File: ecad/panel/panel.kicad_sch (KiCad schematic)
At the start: 201 parts, among them J1 10145226-0241N13LF, J2 Conn_01x03_Pin, J3 USB4105-GF-A, J4 5017868090, SW1 SW_SPDT, SW10 SW_SPDT, SW11 SW_SPDT, SW12 SW_SPDT, SW13 SW_SPDT, SW14 SW_SPDT, SW15 SW_SPDT, SW16 SW_SPDT, SW17 SW_Push, SW18 SW_Push, SW19 SW_Push, SW2 SW_SPDT, SW20 SW_Push, SW21 SW_Push, SW22 SW_Push, SW23 SW_Push, SW24 SW_Push, SW25 SW_Push, SW26 SW_Push, SW27 SW_Push, SW28 SW_Push, SW29 SW_Push, SW3 SW_SPDT, SW30 SW_Push, SW31 SW_Push, SW4 SW_SPDT, SW5 SW_SPDT, SW6 SW_SPDT, SW7 SW_SPDT, SW8 SW_SPDT, SW9 SW_SPDT, U1 TLC59211IN, U2 TLC59211IN, U3 TLC59211IN, U4 TLC59211IN, U5 TLC59211IN, U6 RP2350_80QFN, U7 W25Q128JVS, U8 MCP23017_SO, U9 MCP23017_SO, X1 ABM8-272-T3

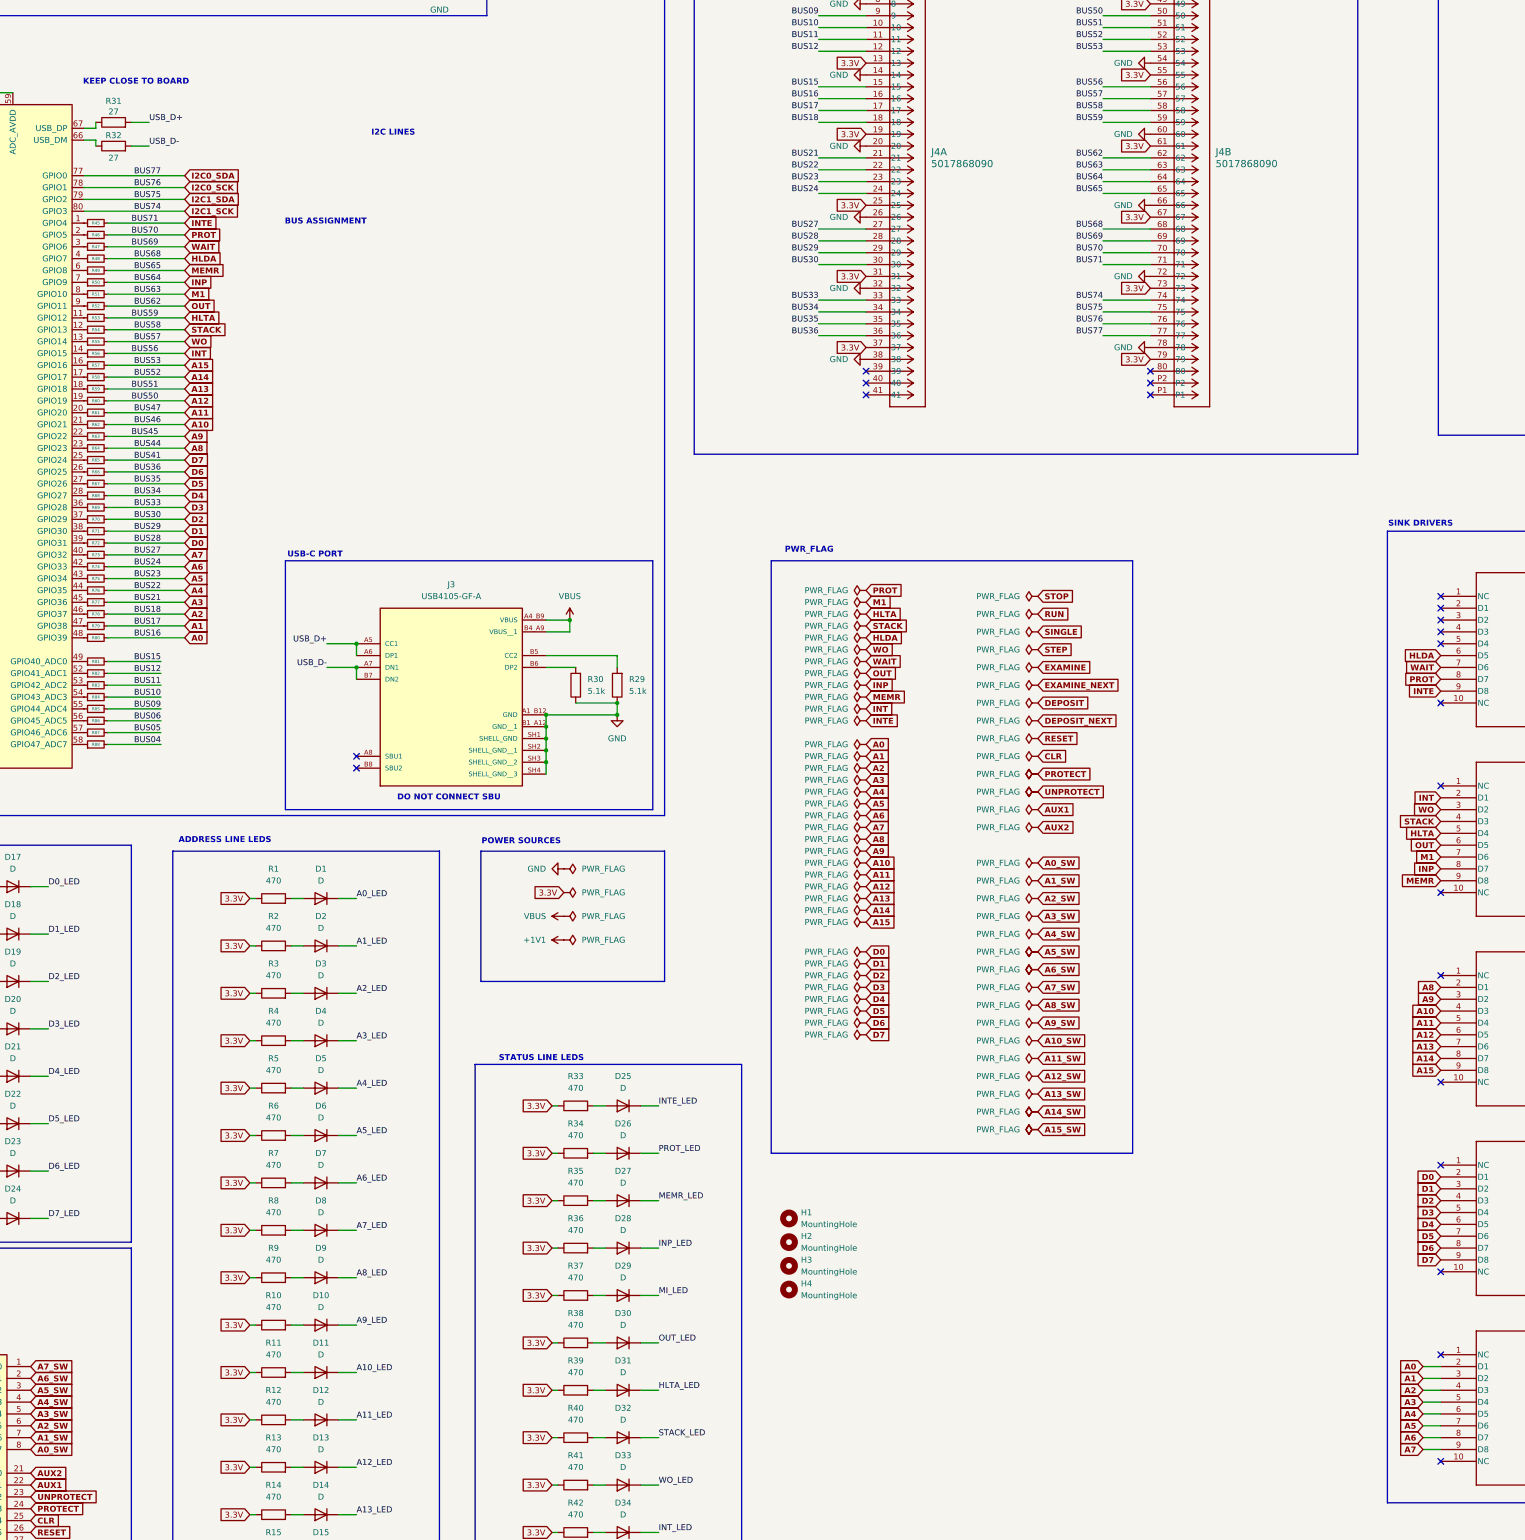
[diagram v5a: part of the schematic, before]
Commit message: remap changes, various card panel fixes
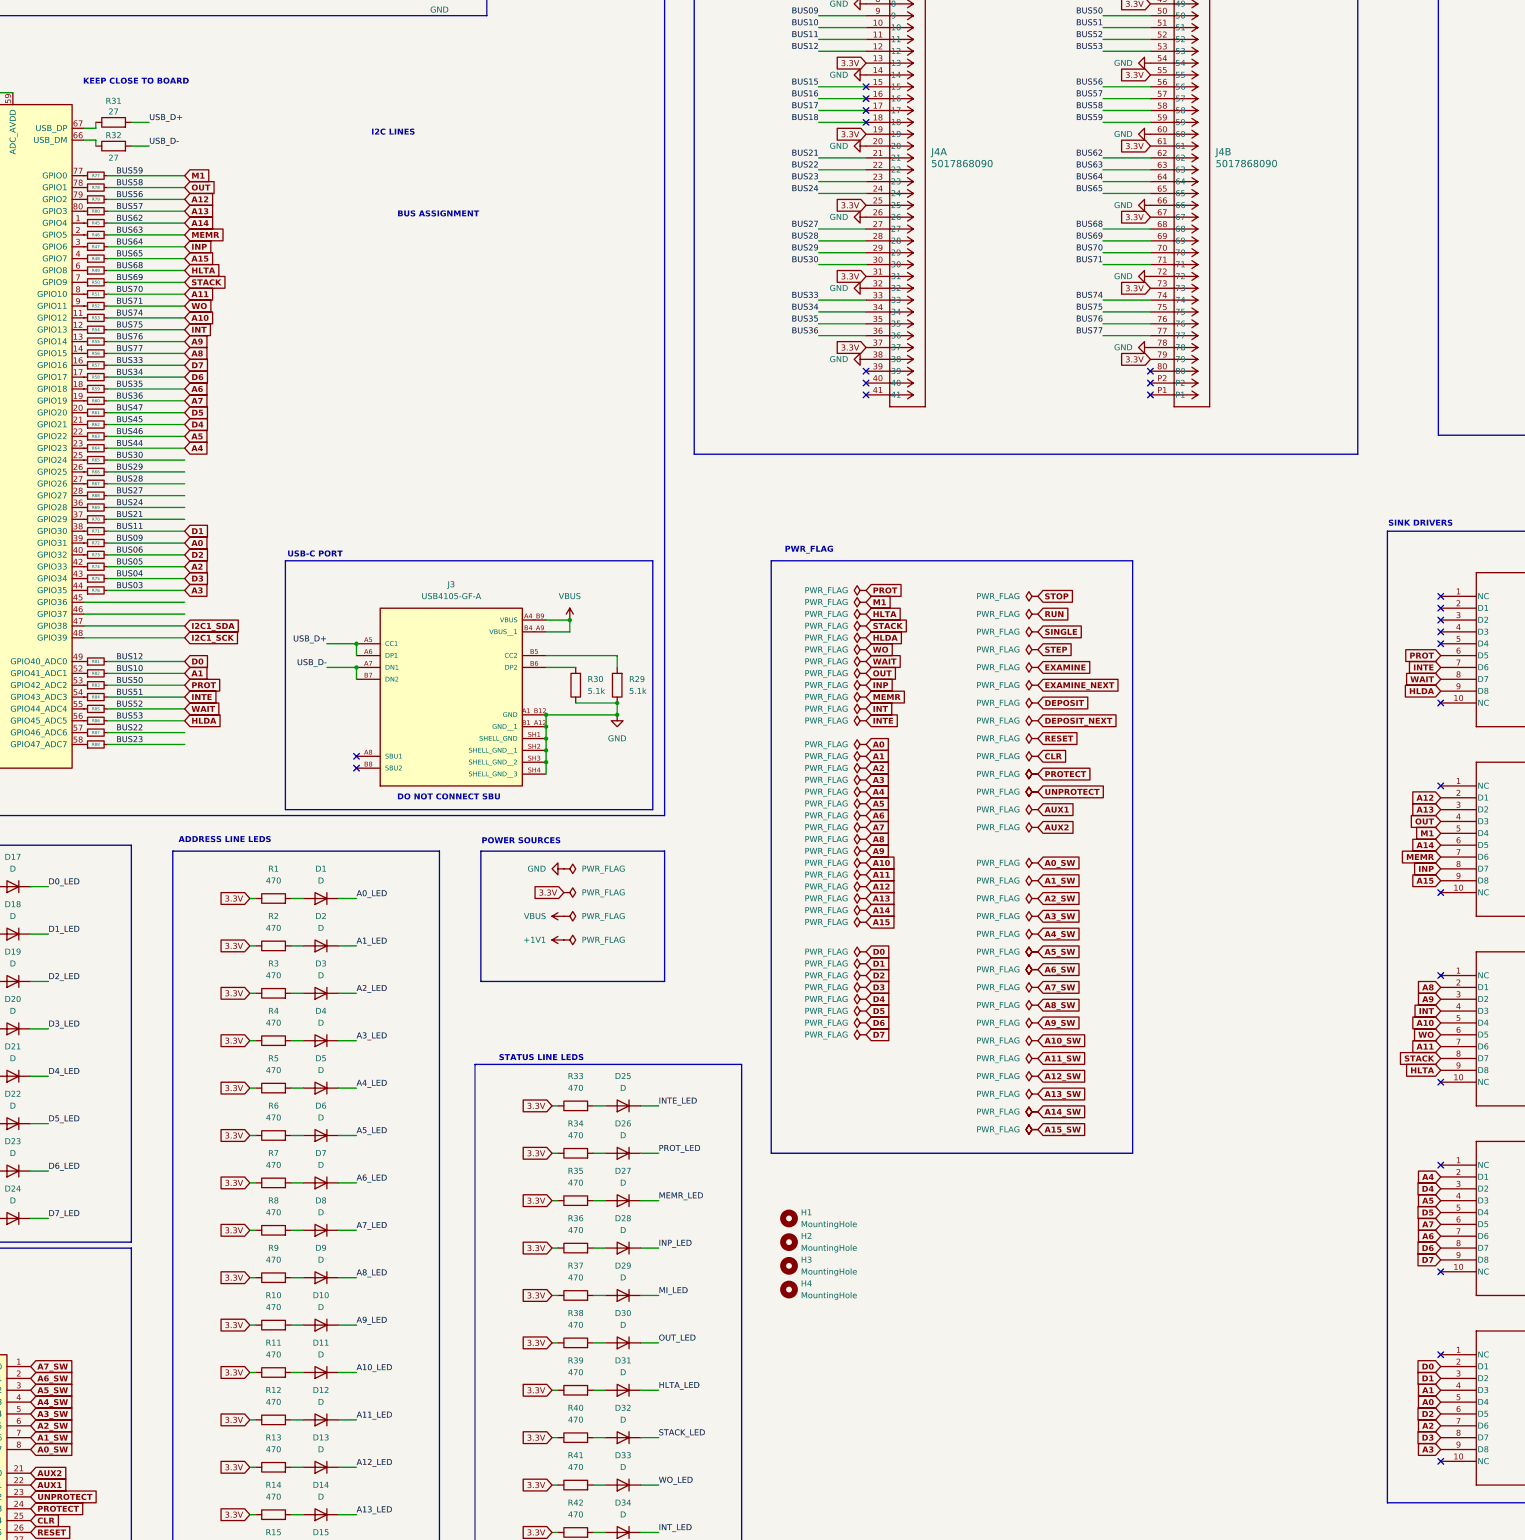
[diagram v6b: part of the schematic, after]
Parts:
- C7, C8: footprint Capacitor_SMD:C_0603_1608Metric -> Capacitor_SMD:C_0402_1005Metric
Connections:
- net BUS03 is gone; now on net A3: J4.3
- net A0: now also J4.9, R72.2, U5.5 (D4); no longer J4.16, R80.2, U5.2 (D1)
- net A1: now also J4.10, R82.2, U5.4 (D3); no longer J4.17, R79.2, U5.3 (D2)
- net A10: now also J4.74, R53.2, U3.5 (D4); no longer J4.46, R62.2, U3.4 (D3)
- net A11: now also J4.70, R51.2, U3.7 (D6); no longer J4.47, R61.2, U3.5 (D4)
- net A12: now also J4.56, R79.2, U2.2 (D1); no longer J4.50, R60.2, U3.6 (D5)
- net A13: now also J4.57, R80.2, U2.3 (D2); no longer J4.51, R59.2, U3.7 (D6)
- net A14: now also J4.62, R45.2, U2.6 (D5); no longer J4.52, R58.2, U3.8 (D7)
- net A15: now also J4.65, R48.2, U2.9 (D8); no longer J4.53, R57.2, U3.9 (D8)
- net A2: now also J4.5, R74.2, U5.7 (D6); no longer J4.18, R78.2, U5.4 (D3)
- net A3: now also R76.2, U5.9 (D8); no longer J4.21, R77.2, U5.5 (D4)
- net A4: now also J4.44, R64.2, U4.2 (D1); no longer J4.22, R76.2, U5.6 (D5)
- net A5: now also J4.46, R63.2, U4.4 (D3); no longer J4.23, R75.2, U5.7 (D6)
- net A6: now also J4.35, R59.2, U4.7 (D6); no longer J4.24, R74.2, U5.8 (D7)
- net A7: now also J4.36, R60.2, U4.6 (D5); no longer J4.27, R73.2, U5.9 (D8)
- net A8: now also J4.77, R56.2; no longer J4.44, R64.2
- net A9: now also J4.76, R55.2; no longer J4.45, R63.2
- net BUS15: no longer R81.2
- net D0: now also J4.12, R81.2, U5.2 (D1); no longer J4.28, R72.2, U4.2 (D1)
- net D1: now also J4.11, U5.3 (D2); no longer J4.29, U4.3 (D2)
- net D2: now also J4.6, R73.2, U5.6 (D5); no longer J4.30, R70.2, U4.4 (D3)
- net D3: now also J4.4, R75.2, U5.8 (D7); no longer J4.33, R69.2, U4.5 (D4)
- net D4: now also J4.45, R62.2, U4.3 (D2); no longer J4.34, R68.2, U4.6 (D5)
- net D5: now also J4.47, R61.2, U4.5 (D4); no longer J4.35, R67.2, U4.7 (D6)
- net D6: now also J4.34, R58.2; no longer J4.36, R66.2
- net D7: now also J4.33, R57.2; no longer R65.2
- net HLDA: now also J4.53, R86.2, U1.9 (D8); no longer J4.68, R48.2, U1.6 (D5)
- net HLTA: now also J4.68, R49.2, U3.9 (D8); no longer J4.59, R53.2, U2.5 (D4)
- net I2C0_SCK: no longer J4.76, U6.78 (GPIO1)
- net I2C0_SDA: no longer J4.77, U6.77 (GPIO0)
- net I2C1_SCK: now also U6.48 (GPIO39); no longer J4.74, U6.80 (GPIO3)
- net I2C1_SDA: now also U6.47 (GPIO38); no longer J4.75, U6.79 (GPIO2)
- net INP: now also R47.2; no longer R50.2
- net INT: now also J4.75, R54.2, U3.4 (D3); no longer J4.56, R56.2, U2.2 (D1)
- net INTE: now also J4.51, R84.2, U1.7 (D6); no longer J4.71, R45.2, U1.9 (D8)
- net M1: now also J4.59, R77.2, U2.5 (D4); no longer J4.63, R51.2, U2.7 (D6)
- net MEMR: now also J4.63, R46.2, U2.7 (D6); no longer J4.65, R49.2, U2.9 (D8)
- net OUT: now also J4.58, R78.2, U2.4 (D3); no longer J4.62, R52.2, U2.6 (D5)
- net PROT: now also J4.50, R83.2, U1.6 (D5); no longer J4.70, R46.2, U1.8 (D7)
- net STACK: now also J4.69, R50.2, U3.8 (D7); no longer J4.58, R54.2, U2.4 (D3)
- net WAIT: now also J4.52, R85.2, U1.8 (D7); no longer J4.69, R47.2, U1.7 (D6)
- net WO: now also J4.71, R52.2, U3.6 (D5); no longer J4.57, R55.2, U2.3 (D2)
- net at R80.1: now also U6.80 (GPIO3); no longer U6.48 (GPIO39)
- net at R77.1: now also U6.77 (GPIO0); no longer U6.45 (GPIO36)
- net at R79.1: now also U6.79 (GPIO2); no longer U6.47 (GPIO38)
- net at R78.1: now also U6.78 (GPIO1); no longer U6.46 (GPIO37)
- net BUS04 renamed BUS23
- net BUS23: now also J4.23; no longer J4.4
- net BUS05 renamed BUS22
- net BUS22: now also J4.22; no longer J4.5
- removed net BUS06: J4.6, R86.2
- removed net BUS09: J4.9, R85.2
- removed net BUS10: J4.10, R84.2
- removed net BUS11: J4.11, R83.2
- removed net BUS12: J4.12, R82.2
- new net BUS16: J4.16
- new net BUS17: J4.17
- new net BUS18: J4.18
- new net BUS21: J4.21, R70.2
- new net BUS24: J4.24, R69.2
- new net BUS27: J4.27, R68.2
- new net BUS28: J4.28, R67.2
- new net BUS29: J4.29, R66.2
- new net BUS30: J4.30, R65.2
- no-connect marks 242 -> 246
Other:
- moved on the sheet: R77, R78, R79, R80
